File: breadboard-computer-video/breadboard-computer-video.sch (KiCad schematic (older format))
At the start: 9 parts

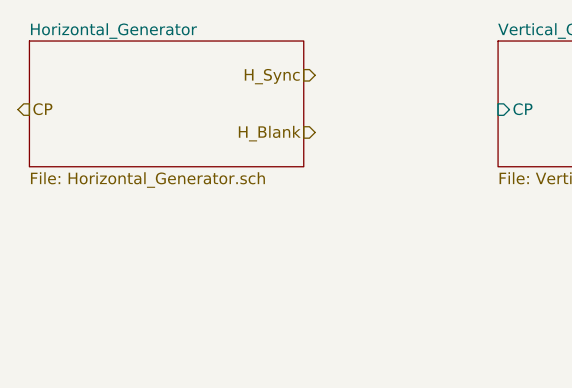
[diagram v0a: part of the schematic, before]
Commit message: Finished H and V generators
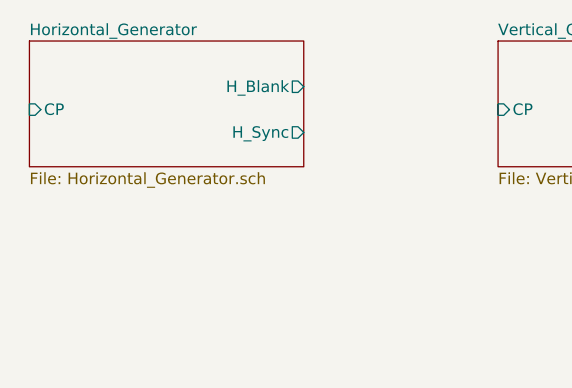
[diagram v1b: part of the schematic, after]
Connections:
- net labels removed: CP, H_Blank, H_Sync
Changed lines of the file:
@@
 F0 "Horizontal_Generator" 50
 F1 "Horizontal_Generator.sch" 50
+F2 "CP" I L 3950 2000 50
+F3 "H_Blank" O R 5150 1900 50
+F4 "H_Sync" O R 5150 2100 50
 $EndSheet
-Text HLabel 3900 2000 2    50   Input ~ 0
-CP
-Text HLabel 5200 1850 0    50   Input ~ 0
-H_Sync
-Text HLabel 5200 2100 0    50   Input ~ 0
-H_Blank
 $EndSCHEMATC

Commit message: Finished sync generation, added pixel clock
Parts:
- added C? (x2): 25pF, symbol Device:C
- added R? (x2): R_US, symbol Device:R_US
- added U? (x2): 74HC04, symbol 74xx:74HC04
- added Y1: 3.640MHz, symbol Device:Crystal
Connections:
- wire segments 24 -> 44
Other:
- moved on the sheet: Q?, R?, U?, U?A

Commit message: added things
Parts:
- removed U?: MCM2513, symbol Character_Generator:MCM2513
- added U?: 74LS161, symbol 74xx:74LS161
- added U?: MCM2513, symbol Character_Generator:MCM2513
- added U?: 74LS08, symbol 74xx:74LS08
- added U?: 74LS32, symbol 74xx:74LS32
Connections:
- net labels added: -12V, -5V, Earth, VCC
- wire segments 44 -> 66
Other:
- moved on the sheet: C?, R?, U?, U?A, U?B, Y1

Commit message: finished
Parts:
- removed U?: 74LS161, symbol 74xx:74LS161
- removed U?: MCM2513, symbol Character_Generator:MCM2513
- added U? (x2): 74LS163, symbol 74xx:74LS163
- added U?: 28C256, symbol Memory_EEPROM:28C256
- added U? (x2): 74LS08, symbol 74xx:74LS08
- added U?: 74LS04, symbol 74xx:74LS04
- added U?: 74LS02, symbol 74xx:74LS02
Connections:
- net labels removed: -12V, -5V
- wire segments 66 -> 158
- no-connect marks 0 -> 12

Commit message: fixed labels
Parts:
- removed U? (x2): 74HC04, symbol 74xx:74HC04
- added U6: 74LS14, symbol 74xx:74LS14
- R1: renamed from R?; value R_US -> 1M
- R2: renamed from R?; value R_US -> 5.6k
- gave numbers to parts that had none: 16
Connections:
- net Horizontal_Generator/CP: now also U6.4
- net at C1.1, R1.2, Y1.1: now also U6.1
- net at R1.1, R2.1: now also U6.2, U6.3
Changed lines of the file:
@@
 $EndComp
 $Comp
-L Device:R_US R?
+L Device:R_US R6
 U 1 1 5D961035
 P 7900 4250
-F 0 "R?" H 7968 4296 50  0000 L CNN
+F 0 "R6" H 7968 4296 50  0000 L CNN
 F 1 "68" H 7968 4205 50  0000 L CNN
 F 2 "" V 7940 4240 50  0001 C CNN
@@
 $EndComp
 $Comp
-L Device:R_US R?
+L Device:R_US R5
 U 1 1 5D9635AA
 P 7900 3950
-F 0 "R?" H 7968 3996 50  0000 L CNN
+F 0 "R5" H 7968 3996 50  0000 L CNN
 F 1 "10" H 7968 3905 50  0000 L CNN
 F 2 "" V 7940 3940 50  0001 C CNN
@@
 	7900 4100 9050 4100
 $Comp
-L Device:Q_NPN_BCE Q?
+L Device:Q_NPN_BCE Q2
 U 1 1 5D965299
 P 7800 3600
-F 0 "Q?" H 7991 3646 50  0000 L CNN
+F 0 "Q2" H 7991 3646 50  0000 L CNN
 F 1 "Q_NPN_BCE" H 7991 3555 50  0000 L CNN
 F 2 "" H 8000 3700 50  0001 C CNN
@@
 Connection ~ 7900 4100
 $Comp
-L Device:Q_NPN_BCE Q?
+L Device:Q_NPN_BCE Q1
 U 1 1 5D969DDB
 P 7800 2850
-F 0 "Q?" H 7991 2896 50  0000 L CNN
+F 0 "Q1" H 7991 2896 50  0000 L CNN
 F 1 "Q_NPN_BCE" H 7991 2805 50  0000 L CNN
 F 2 "" H 8000 2950 50  0001 C CNN
@@
 	7900 3050 7900 3400
 $Comp
-L Device:R_US R?
+L Device:R_US R4
 U 1 1 5D96E054
 P 7300 3750
-F 0 "R?" H 7368 3796 50  0000 L CNN
+F 0 "R4" H 7368 3796 50  0000 L CNN
 F 1 "2.2k" H 7368 3705 50  0000 L CNN
 F 2 "" V 7340 3740 50  0001 C CNN
@@
 $EndComp
 $Comp
-L Device:R_US R?
+L Device:R_US R3
 U 1 1 5D96E923
 P 7150 3600
-F 0 "R?" H 7218 3646 50  0000 L CNN
+F 0 "R3" H 7218 3646 50  0000 L CNN
 F 1 "10k" H 7218 3555 50  0000 L CNN
 F 2 "" V 7190 3590 50  0001 C CNN
@@
 $EndComp
 $Comp
-L 74xx:74LS02 U?
+L 74xx:74LS02 U8
 U 1 1 5D974F6E
 P 7300 2850
-F 0 "U?" H 7300 3175 50  0000 C CNN
+F 0 "U8" H 7300 3175 50  0000 C CNN
 F 1 "74LS02" H 7300 3084 50  0000 C CNN
 F 2 "" H 7300 2850 50  0001 C CNN
@@
 	6650 1700 6650 2950
 $Comp
-L 74xx:74HC04 U?
-U 1 1 5D9A9DE2
-P 3700 1600
-F 0 "U?" H 3700 1917 50  0000 C CNN
-F 1 "74HC04" H 3700 1826 50  0000 C CNN
-F 2 "" H 3700 1600 50  0001 C CNN
-F 3 "https://assets.nexperia.com/documents/data-sheet/74HC_HCT04.pdf" H 3700 1600 50  0001 C CNN
-	1    3700 1600
-	1    0    0    -1
-$EndComp
-$Comp
-L 74xx:74HC04 U?
-U 2 1 5D9AAB16
-P 4500 1600
-F 0 "U?" H 4500 1917 50  0000 C CNN
-F 1 "74HC04" H 4500 1826 50  0000 C CNN
-F 2 "" H 4500 1600 50  0001 C CNN
-F 3 "https://assets.nexperia.com/documents/data-sheet/74HC_HCT04.pdf" H 4500 1600 50  0001 C CNN
-	2    4500 1600
-	1    0    0    -1
-$EndComp
-$Comp
-L Device:C C?
+L Device:C C1
 U 1 1 5D9AD126
 P 3300 3000
-F 0 "C?" H 3415 3046 50  0000 L CNN
+F 0 "C1" H 3415 3046 50  0000 L CNN
 F 1 "25pF" H 3415 2955 50  0000 L CNN
 F 2 "" H 3338 2850 50  0001 C CNN
@@
 $EndComp
 $Comp
-L Device:C C?
+L Device:C C2
 U 1 1 5D9ADB4B
 P 4100 3000
-F 0 "C?" H 4215 3046 50  0000 L CNN
+F 0 "C2" H 4215 3046 50  0000 L CNN
 F 1 "25pF" H 4215 2955 50  0000 L CNN
 F 2 "" H 4138 2850 50  0001 C CNN
@@
 $EndComp
 $Comp
-L Device:R_US R?
+L Device:R_US R2
 U 1 1 5D9AF295
 P 4100 2400
-F 0 "R?" H 4168 2446 50  0000 L CNN
-F 1 "R_US" H 4168 2355 50  0000 L CNN
+F 0 "R2" H 4168 2446 50  0000 L CNN
+F 1 "5.6k" H 4168 2355 50  0000 L CNN
 F 2 "" V 4140 2390 50  0001 C CNN
 F 3 "~" H 4100 2400 50  0001 C CNN
@@
 $EndComp
 $Comp
-L Device:R_US R?
+L Device:R_US R1
 U 1 1 5D9AFC84
 P 3700 2150
-F 0 "R?" V 3495 2150 50  0000 C CNN
-F 1 "R_US" V 3586 2150 50  0000 C CNN
+F 0 "R1" V 3495 2150 50  0000 C CNN
+F 1 "1M" V 3586 2150 50  0000 C CNN
 F 2 "" V 3740 2140 50  0001 C CNN
 F 3 "~" H 3700 2150 50  0001 C CNN
@@
 	4200 5200 3400 5200
 $Comp
-L 74xx:74LS08 U?
+L 74xx:74LS08 U4
 U 1 1 5DBCD2DA
 P 3300 6900
-F 0 "U?" V 3254 7088 50  0000 L CNN
+F 0 "U4" V 3254 7088 50  0000 L CNN
 F 1 "74LS08" V 3345 7088 50  0000 L CNN
 F 2 "" H 3300 6900 50  0001 C CNN
@@
 	1950 6200 1950 6450
 $Comp
-L 74xx:74LS32 U?
+L 74xx:74LS32 U3
 U 1 1 5DC0297B
 P 1950 6750
-F 0 "U?" V 1996 6570 50  0000 R CNN
+F 0 "U3" V 1996 6570 50  0000 R CNN
 F 1 "74LS32" V 1905 6570 50  0000 R CNN
 F 2 "" H 1950 6750 50  0001 C CNN
@@
 	3400 5200 3400 5400
 $Comp
-L 74xx:74LS163 U?
+L 74xx:74LS163 U5
 U 1 1 5E0B242E
 P 2450 5700
-F 0 "U?" H 2450 6681 50  0000 C CNN
+F 0 "U5" H 2450 6681 50  0000 C CNN
 F 1 "74LS163" H 2450 6590 50  0000 C CNN
 F 2 "" H 2450 5700 50  0001 C CNN
@@
 $EndSheet
 $Comp
-L Memory_EEPROM:28C256 U?
+L Memory_EEPROM:28C256 U7
 U 1 1 5E1F0F95
 P 4600 6100
-F 0 "U?" H 4600 7381 50  0000 C CNN
+F 0 "U7" H 4600 7381 50  0000 C CNN
 F 1 "28C256" H 4600 7290 50  0000 C CNN
 F 2 "" H 4600 6100 50  0001 C CNN
@@
 	4600 7550 5800 7550
 $Comp
-L 4xxx:4021 U?
+L 4xxx:4021 U9
 U 1 1 5D92BCAE
 P 6600 4500
-F 0 "U?" H 6600 5481 50  0000 C CNN
+F 0 "U9" H 6600 5481 50  0000 C CNN
 F 1 "4021" H 6600 5390 50  0000 C CNN
 F 2 "" H 6600 4650 50  0001 C CNN
@@
 	800  3450 900  3450
 $Comp
-L 74xx:74LS163 U?
+L 74xx:74LS163 U2
 U 1 1 5E36C15A
 P 1950 2200
-F 0 "U?" V 1904 3044 50  0000 L CNN
+F 0 "U2" V 1904 3044 50  0000 L CNN
 F 1 "74LS163" V 1995 3044 50  0000 L CNN
 F 2 "" H 1950 2200 50  0001 C CNN
@@
 	1650 1000 700  1000
 $Comp
-L 74xx:74LS08 U?
+L 74xx:74LS08 U4
 U 2 1 5E37DDE5
 P 2350 1400
-F 0 "U?" V 2396 1220 50  0000 R CNN
+F 0 "U4" V 2396 1220 50  0000 R CNN
 F 1 "74LS08" V 2305 1220 50  0000 R CNN
 F 2 "" H 2350 1400 50  0001 C CNN
@@
 NoConn ~ 1950 2700
 $Comp
-L 74xx:74LS04 U?
+L 74xx:74LS04 U1
 U 3 1 5E3AF993
 P 1450 1400
-F 0 "U?" V 1404 1580 50  0000 L CNN
+F 0 "U1" V 1404 1580 50  0000 L CNN
 F 1 "74LS04" V 1495 1580 50  0000 L CNN
 F 2 "" H 1450 1400 50  0001 C CNN
@@
 $EndComp
 $Comp
-L 74xx:74LS08 U?
+L 74xx:74LS08 U4
 U 3 1 5E99B421
 P 6700 3600
-F 0 "U?" H 6700 3925 50  0000 C CNN
+F 0 "U4" H 6700 3925 50  0000 C CNN
 F 1 "74LS08" H 6700 3834 50  0000 C CNN
 F 2 "" H 6700 3600 50  0001 C CNN
@@
 	6550 900  800  900
 $Comp
-L 74xx:74LS02 U?
+L 74xx:74LS02 U8
 U 2 1 5E9FFB0B
 P 6200 3050
-F 0 "U?" V 6154 3238 50  0000 L CNN
+F 0 "U8" V 6154 3238 50  0000 L CNN
 F 1 "74LS02" V 6245 3238 50  0000 L CNN
 F 2 "" H 6200 3050 50  0001 C CNN
@@
 	0    1    1    0
 $EndComp
+$Comp
+L 74xx:74LS14 U6
+U 1 1 5EA1FAA0
+P 3700 1600
+F 0 "U6" H 3700 1917 50  0000 C CNN
+F 1 "74LS14" H 3700 1826 50  0000 C CNN
+F 2 "" H 3700 1600 50  0001 C CNN
+F 3 "http://www.ti.com/lit/gpn/sn74LS14" H 3700 1600 50  0001 C CNN
+	1    3700 1600
+	1    0    0    -1
+$EndComp
+$Comp
+L 74xx:74LS14 U6
+U 2 1 5EA2147E
+P 4500 1600
+F 0 "U6" H 4500 1917 50  0000 C CNN
+F 1 "74LS14" H 4500 1826 50  0000 C CNN
+F 2 "" H 4500 1600 50  0001 C CNN
+F 3 "http://www.ti.com/lit/gpn/sn74LS14" H 4500 1600 50  0001 C CNN
+	2    4500 1600
+	1    0    0    -1
+$EndComp
 $EndSCHEMATC
